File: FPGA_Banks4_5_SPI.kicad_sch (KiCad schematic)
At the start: 6 parts, among them U1 NX1H35 PBGA625, U4 AS4C8M16SA-6BIN

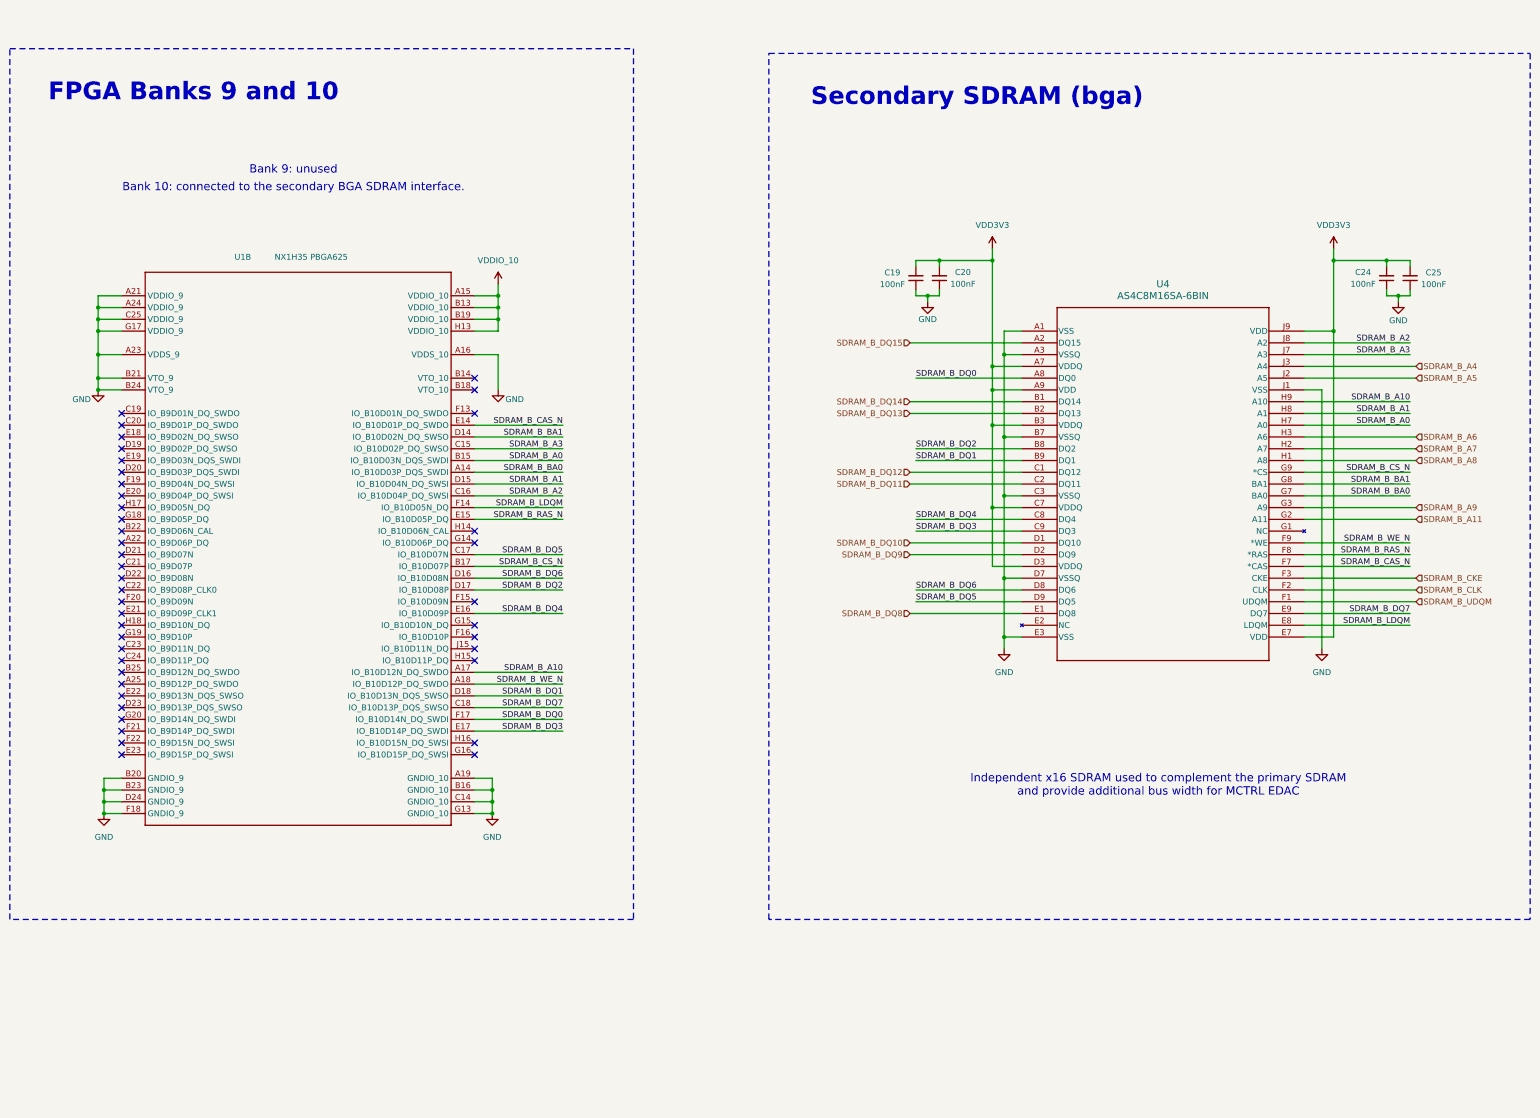
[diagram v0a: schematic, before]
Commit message: pre order checks
ADDED jumper for VDDSENSE remote sensing / 1V2 core PWR for MAX LDO feedback
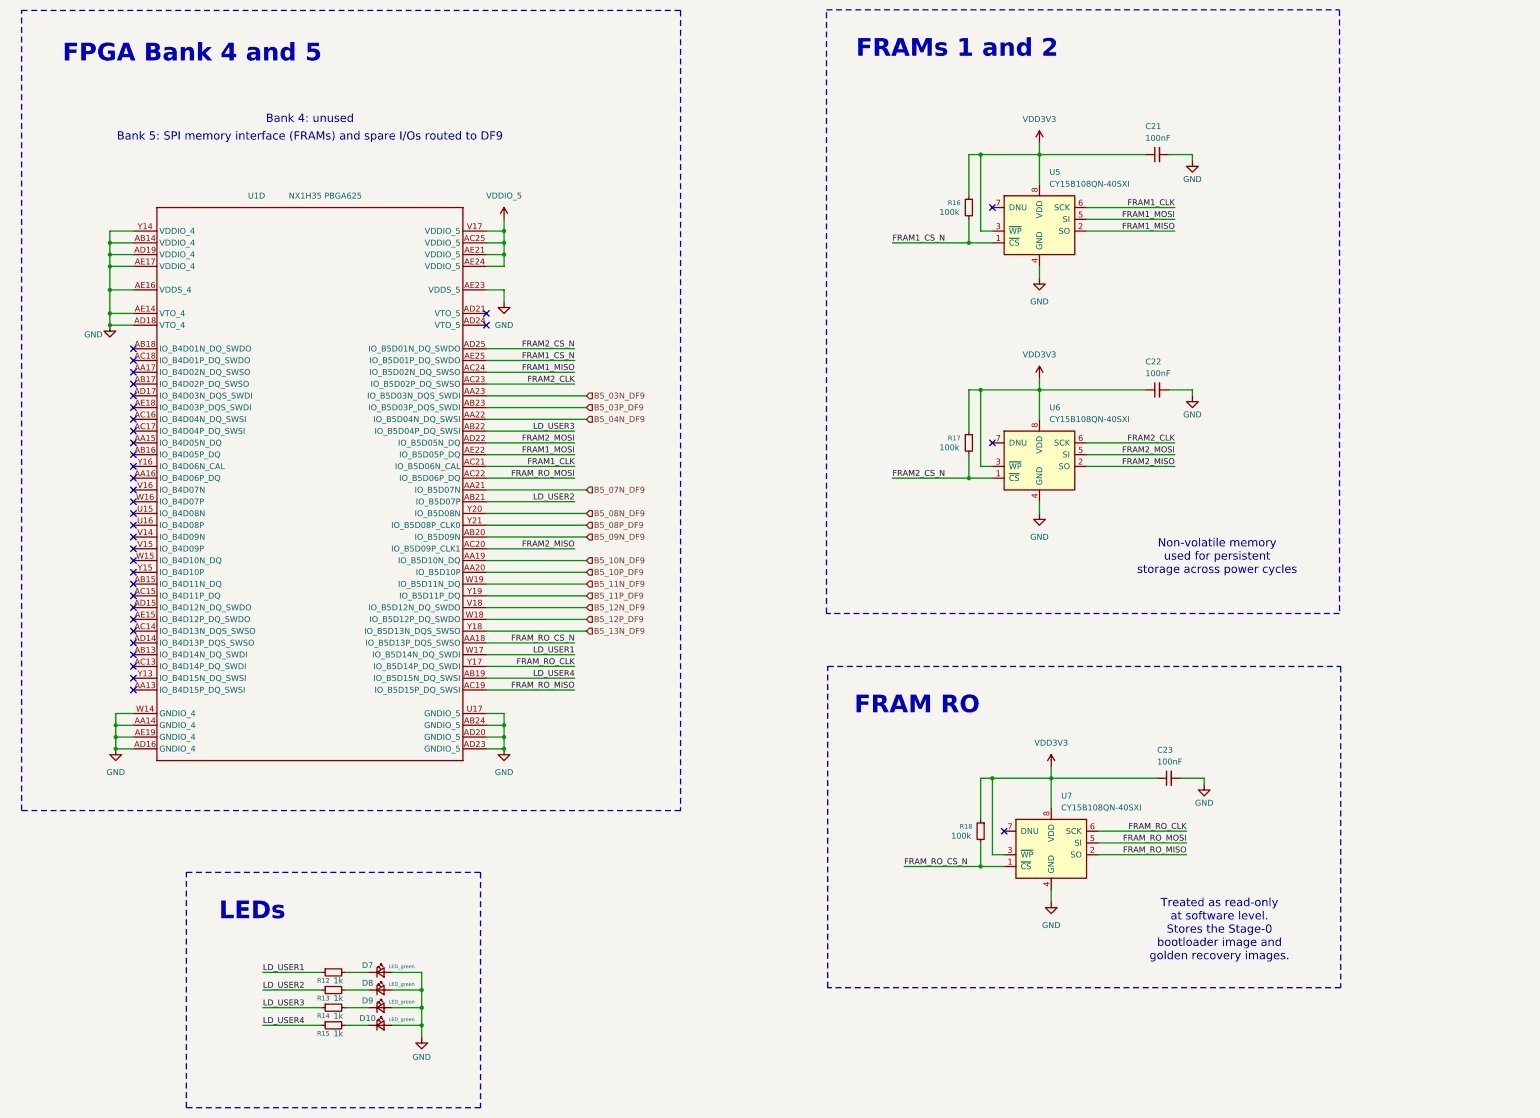
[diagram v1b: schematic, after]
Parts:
- removed C19, C20, C24, C25: 100nF, Capacitor_SMD:C_0402_1005Metric_Pad0.74x0.62mm_HandSolder, symbol Device:C_Small
- removed U1: NX1H35 PBGA625, DataHub_NG_Medium:NX1H35S_CLGA625, symbol Brave625:root_0_BRAVE625A_Brave625.SchLib
- removed U4: AS4C8M16SA-6BIN, DataHub_Footprints:sdram2_bga_TFBGA-54_8X8_ALL, symbol SDRAM_BGA_8x16:AS4C8M16S-6BIN
- added C21, C22, C23: 100nF, Capacitor_SMD:C_0402_1005Metric_Pad0.74x0.62mm_HandSolder, symbol Device:C_Small
- added D10, D7, D8, D9: LED_green, LED_SMD:LED_0603_1608Metric, symbol Device:LED_Small
- added R12, R13, R14, R15: 1k, Resistor_SMD:R_0402_1005Metric_Pad0.72x0.64mm_HandSolder, symbol Device:R_Small
- added R16, R17, R18: 100k, Resistor_SMD:R_0402_1005Metric_Pad0.72x0.64mm_HandSolder, symbol Device:R_Small
- added U1: NX1H35 PBGA625, DataHub_NG_Medium:NX1H35S_CLGA625, symbol Brave625:root_0_BRAVE625A_Brave625.SchLib
- added U5, U6, U7: CY15B108QN-40SXI, DataHub_Footprints:SOIC8_001-85261_CYP, symbol Memory_NVRAM:MB85RS1MT
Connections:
- net GND: now also C21.2, C22.2, C23.2, D10.2 (A), D7.2 (A), D8.2 (A), D9.2 (A), U1.AA14 (GNDIO_4), U1.AB14 (VDDIO_4), U1.AB24 (GNDIO_5), U1.AD16 (GNDIO_4), U1.AD18 (VTO_4), U1.AD19 (VDDIO_4), U1.AD20 (GNDIO_5), U1.AD23 (GNDIO_5), U1.AE14 (VTO_4), U1.AE16 (VDDS_4), U1.AE17 (VDDIO_4), U1.AE19 (GNDIO_4), U1.AE23 (VDDS_5), U1.U17 (GNDIO_5), U1.W14 (GNDIO_4), U1.Y14 (VDDIO_4), U5.4 (GND), U6.4 (GND), U7.4 (GND)
- net VDD3V3: now also C21.1, C22.1, C23.1, R16.1, R17.1, R18.1, U5.3 (~{WP}), U5.8 (VDD), U6.3 (~{WP}), U6.8 (VDD), U7.3 (~{WP}), U7.8 (VDD)
- new net: D7.1 (K), R12.2
- new net: D8.1 (K), R13.2
- new net: D9.1 (K), R14.2
- new net: D10.1 (K), R15.2
- new net B5_03N_DF9: U1.AA23 (IO_B5D03N_DQS_SWDI)
- new net B5_03P_DF9: U1.AB23 (IO_B5D03P_DQS_SWDI)
- new net B5_04N_DF9: U1.AA22 (IO_B5D04N_DQ_SWSI)
- new net B5_07N_DF9: U1.AA21 (IO_B5D07N)
- new net B5_08N_DF9: U1.Y20 (IO_B5D08N)
- new net B5_08P_DF9: U1.Y21 (IO_B5D08P_CLK0)
- new net B5_09N_DF9: U1.AB20 (IO_B5D09N)
- new net B5_10N_DF9: U1.AA19 (IO_B5D10N_DQ)
- new net B5_10P_DF9: U1.AA20 (IO_B5D10P)
- new net B5_11N_DF9: U1.W19 (IO_B5D11N_DQ)
- new net B5_11P_DF9: U1.Y19 (IO_B5D11P_DQ)
- new net B5_12N_DF9: U1.V18 (IO_B5D12N_DQ_SWDO)
- new net B5_12P_DF9: U1.W18 (IO_B5D12P_DQ_SWDO)
- new net B5_13N_DF9: U1.Y18 (IO_B5D13N_DQS_SWSO)
- new net FRAM1_CLK: U1.AC21 (IO_B5D06N_CAL), U5.6 (SCK)
- new net FRAM1_CS_N: R16.2, U1.AE25 (IO_B5D01P_DQ_SWDO), U5.1 (~{CS})
- new net FRAM1_MISO: U1.AC24 (IO_B5D02N_DQ_SWSO), U5.2 (SO)
- new net FRAM1_MOSI: U1.AE22 (IO_B5D05P_DQ), U5.5 (SI)
- new net FRAM2_CLK: U1.AC23 (IO_B5D02P_DQ_SWSO), U6.6 (SCK)
- new net FRAM2_CS_N: R17.2, U1.AD25 (IO_B5D01N_DQ_SWDO), U6.1 (~{CS})
- new net FRAM2_MISO: U1.AC20 (IO_B5D09P_CLK1), U6.2 (SO)
- new net FRAM2_MOSI: U1.AD22 (IO_B5D05N_DQ), U6.5 (SI)
- new net FRAM_RO_CLK: U1.Y17 (IO_B5D14P_DQ_SWDI), U7.6 (SCK)
- new net FRAM_RO_CS_N: R18.2, U1.AA18 (IO_B5D13P_DQS_SWSO), U7.1 (~{CS})
- new net FRAM_RO_MISO: U1.AC19 (IO_B5D15P_DQ_SWSI), U7.2 (SO)
- new net FRAM_RO_MOSI: U1.AC22 (IO_B5D06P_DQ), U7.5 (SI)
- new net LD_USER1: R12.1, U1.W17 (IO_B5D14N_DQ_SWDI)
- new net LD_USER2: R13.1, U1.AB21 (IO_B5D07P)
- new net LD_USER3: R14.1, U1.AB22 (IO_B5D04P_DQ_SWSI)
- new net LD_USER4: R15.1, U1.AB19 (IO_B5D15N_DQ_SWSI)
- new net VDDIO_5: U1.AC25 (VDDIO_5), U1.AE21 (VDDIO_5), U1.AE24 (VDDIO_5), U1.V17 (VDDIO_5)
- no-connect marks 42 -> 35
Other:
- note added: "Bank 4: unused"
- note added: "Bank 5: SPI memory interface (FRAMs) and spare I/Os routed to DF9"
- note added: "FPGA Bank 4 and 5"
- note added: "FRAM RO"
- note added: "FRAMs 1 and 2"
- note added: "LEDs"
- note added: "Non-volatile memory used for persistent storage across power cycles"
- note added: "Treated as read-only at software level. Stores the Stage-0 bootloader image and golden recovery images."
- note removed: "Bank 10: connected to the secondary BGA SDRAM interface."
- note removed: "Bank 9: unused"
- note removed: "FPGA Banks 9 and 10"
- note removed: "Independent x16 SDRAM used to complement the primary SDRAM and provide additional bus width for MCTRL EDAC"
- note removed: "Secondary SDRAM (bga)"
- company: (none) -> KTH Royal Institute of Technology
- title: (none) -> SPI Memory Interface - FPGA Banks 4 and 5
